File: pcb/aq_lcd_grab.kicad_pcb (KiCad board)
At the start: 4 copper layers, 32 x 50 mm, 29 parts, among them J1 Conn_01x39_Socket, J2 Conn_01x39_Socket, J3 Conn_01x03_Socket, J4 Conn_01x02_Socket, J5 Conn_01x03_Pin, U1 STM32F103C8Tx, U2 Conn_01x14

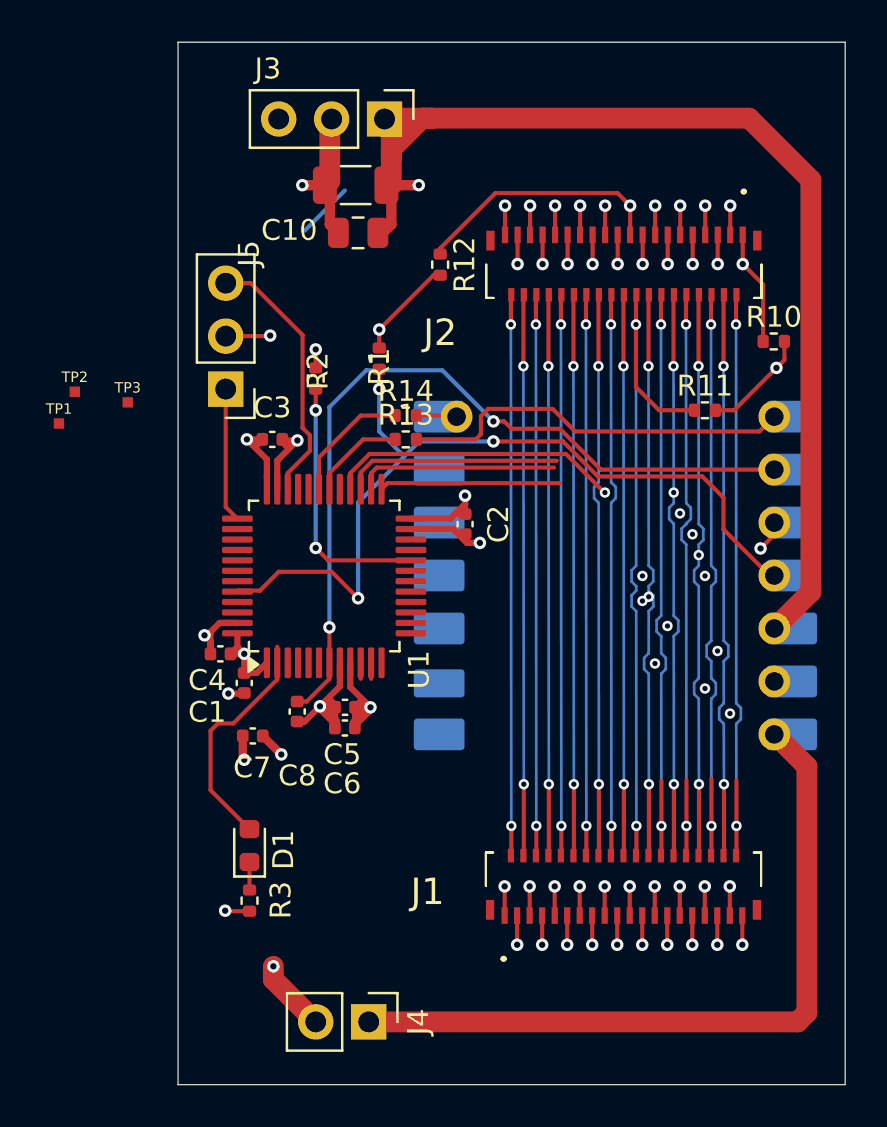
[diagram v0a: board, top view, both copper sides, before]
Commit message: pcb: test points on PA6/7/8; STM32 PA11 as second PIC32 reset driver
- Replace test-point cluster (was PB3/PB4/PA6, required JTAG disable)
  with PA6/PA7/PA8 (pads 16/17/29) — all plain GPIO, no AF conflicts.

- Add STM32 PA11 (pad 32) as a second open-drain driver for PIC32 reset,
  mirroring the existing ESP32 GPIO20 path.  Both drivers wire through
  individual 0 Ω jumpers (R15 = ESP32 side, R16 = STM32 side) onto the
  shared PIC32_RESET net at J3 pin 3; break a jumper to isolate that
  driver without cutting the other.

- Regen netlist and update KiCad PCB with new footprints / net names.

- route_lcd_bus.py: rework escape-via placement (drop odd_db_escape_y
  helper, consolidate into EXTRA_ESCAPE_VIAS with base+step arithmetic).

Co-Authored-By: Claude Sonnet 4.6 <noreply@anthropic.com>
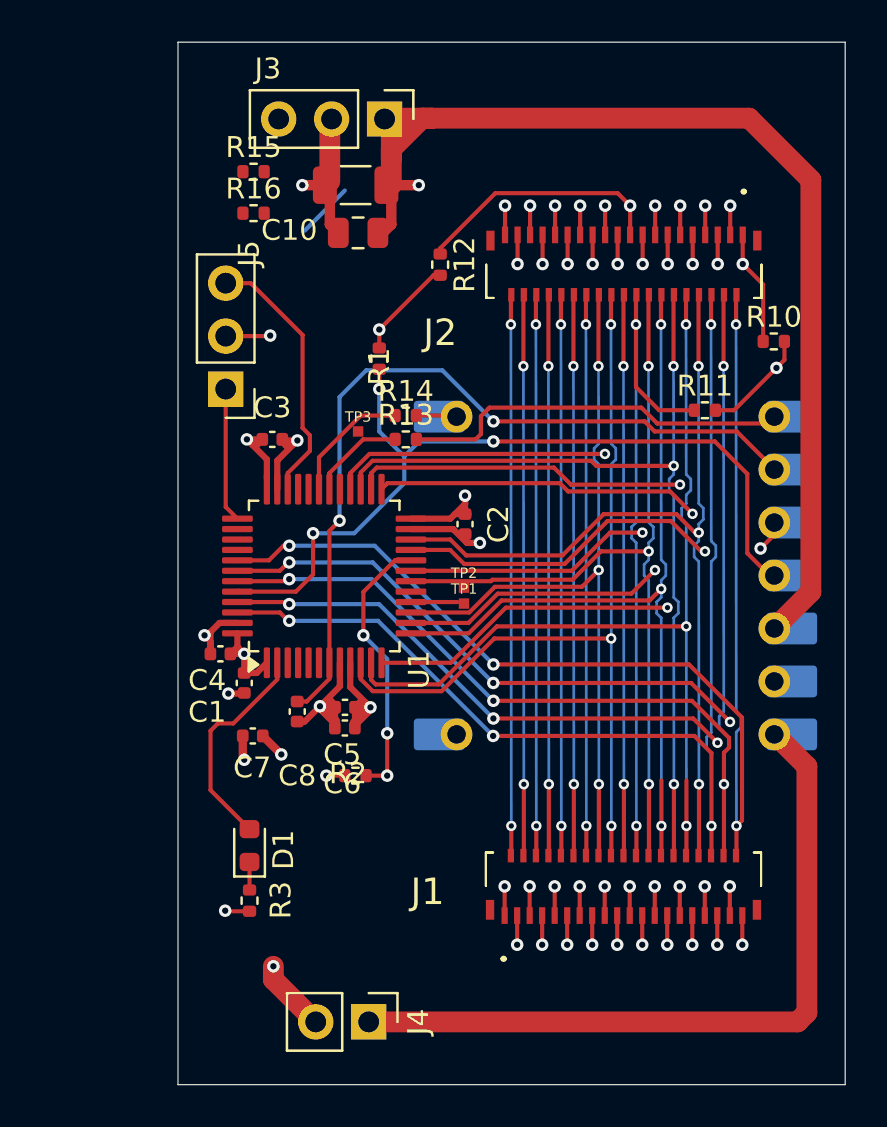
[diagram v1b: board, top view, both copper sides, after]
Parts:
- added R15: 0, Resistor_SMD:R_0402_1005Metric, F.Cu at (54.4, 31.6)
- added R16: 0, Resistor_SMD:R_0402_1005Metric, F.Cu at (54.4, 33.6)
- moved TP1 21.3 mm to (64.5, 52.3)
- moved TP2 20.9 mm to (64.5, 51.6)
- moved R2 19.1 mm to (59.3, 60.6), turned to 180 degrees
- moved TP3 11.1 mm to (59.4, 44.1)
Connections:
- TP1 pad 1: PB3 -> PA6
- TP2 pad 1: PB4 -> PA7
- TP3 pad 1: PA6 -> PA8
- U1 pad 17: (no net) -> PA7
- U1 pad 29: (no net) -> PA8
- U1 pad 32: (no net) -> PIC32_RST_STM
- U1 pad 39: PB3 -> (no net)
- U1 pad 40: PB4 -> (no net)
- U2 pad 10: PIC32_RESET -> PIC32_RST_ESP
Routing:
- net DB0: track 29.3 -> 60.3 mm, vias 2 -> 4
- net DB2: track 27.0 -> 55.9 mm, vias 2 -> 4
- net DB1: track 36.1 -> 63.1 mm, vias 3 -> 5
- net DB4: track 29.7 -> 56.2 mm, vias 2 -> 4
- net DB3: track 36.1 -> 62.0 mm, vias 3 -> 5
- net DB8: track 30.2 -> 46.6 mm, vias 2 -> 3
- net DB5: track 36.3 -> 52.1 mm, vias 4 -> 3
- net DB6: track 27.0 -> 42.2 mm
- net DB11: track 36.3 -> 51.3 mm
- net WR: track 27.8 -> 41.1 mm, vias 2 -> 3
- net DB13: track 36.3 -> 49.2 mm
- net DB12: track 29.4 -> 42.3 mm, vias 2 -> 3
- net DB15: track 36.3 -> 48.2 mm, vias 4 -> 3
- net DB14: track 27.0 -> 38.8 mm
- net CS: track 26.6 -> 36.5 mm, vias 2 -> 3
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
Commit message: pcb: place tooling holes, logo, v1 label; add logo footprint library
- H1–H4 tooling holes placed at board corners (1.152 mm, JLCPCB spec).
- logo:logo-1cm placed on silkscreen.
- v1-<hash> label added to F.SilkS.
- logo.pretty/ added to repo and registered in fp-lib-table.
- kicad_pro: suppress DRC warnings for silk overlap/text height/thickness
  (logo footprint triggers these by design).

Co-Authored-By: Claude Sonnet 4.6 <noreply@anthropic.com>
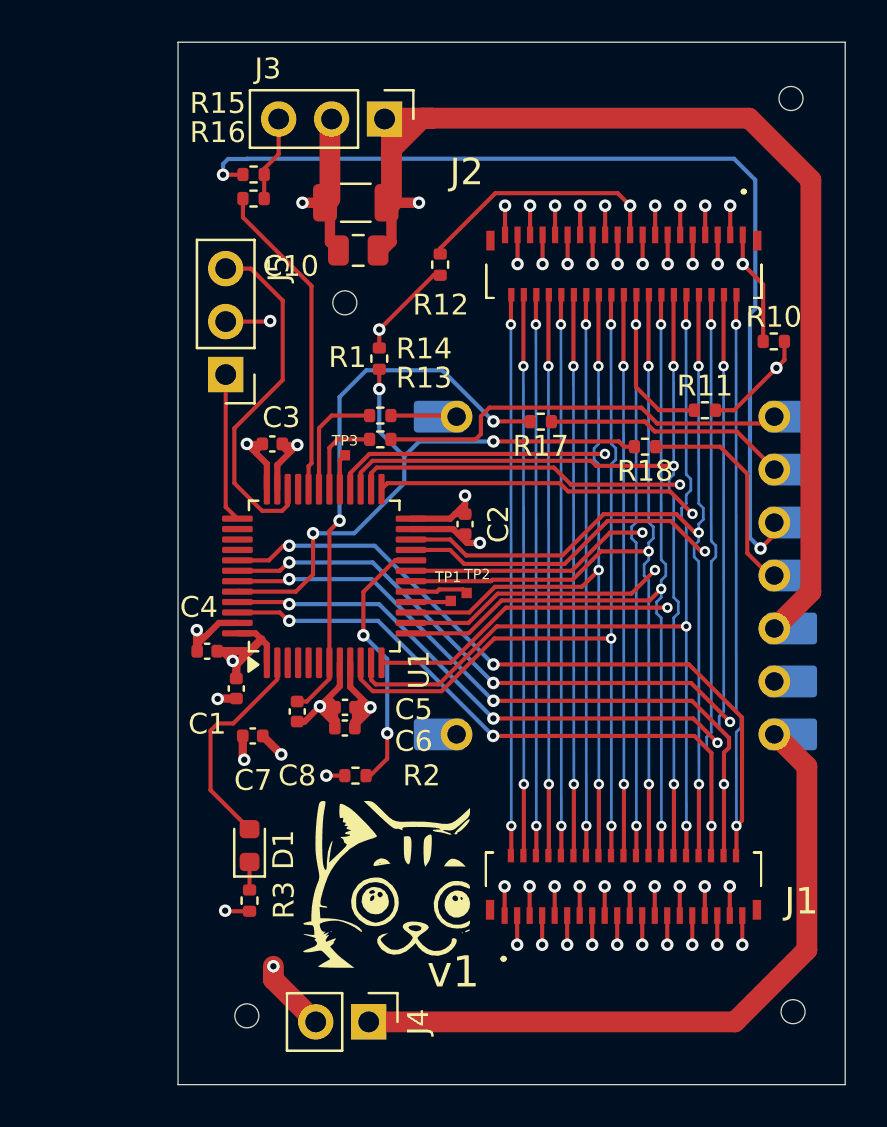
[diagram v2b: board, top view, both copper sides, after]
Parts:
- added H1: ToolingHole, MountingHole:ToolingHole_1.152mm, F.Cu at (58.8, 37.9)
- added H2: ToolingHole, MountingHole:ToolingHole_1.152mm, F.Cu at (54.1, 72.1)
- added H3: ToolingHole, MountingHole:ToolingHole_1.152mm, F.Cu at (80.2, 28.1)
- added H4: ToolingHole, MountingHole:ToolingHole_1.152mm, F.Cu at (80.3, 71.9)
- added R17: 0, Resistor_SMD:R_0402_1005Metric, F.Cu at (68.2, 43.6)
- added R18: 0, Resistor_SMD:R_0402_1005Metric, F.Cu at (73.2, 44.8)
- added v1: LOGO, logo:logo-8mm, F.Cu at (60.8, 65.8)
- added v1: LOGO, logo:logo-2cm, B.Cu at (67.1, 57.5)
- D1: value GREEN -> KT-0603R
- J1, J2: value Conn_01x39_Socket -> FH26W-39S-0.3SHW(60)
- U1: value STM32F103C8Tx -> STM32F103C8T6
- moved TP3 1.31 mm to (58.8, 45.2)
- moved R13 1.22 mm to (60.5, 44.5)
- moved R14 1.22 mm to (60.5, 43.3)
- moved C10 0.84 mm to (59.4, 35.4)
- moved C11 0.84 mm to (59.3, 33.1)
- moved R16 0.70 mm to (54.4, 32.9)
- moved J5 0.70 mm to (53.1, 41.3)
- moved TP1 0.65 mm to (63.9, 52.2)
- moved C4 0.65 mm to (52.2, 54.6)
- moved C1 0.46 mm to (53.6, 56.4)
- moved TP2 0.28 mm to (64.6, 51.8)
- moved C3 0.22 mm to (55.3, 44.7)
- moved R15 0.13 mm to (54.4, 31.7)
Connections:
- U2 pad 11: BOOT0 -> BOOT0_ESP
- U2 pad 9: NRST -> NRST_ESP
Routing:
- net PIC32_RST_ESP: track 1.52 -> 47.0 mm, vias 1 -> 2
- net PIC32_RST_STM: track 0.00 -> 15.4 mm
- net NRST: track 39.1 -> 26.4 mm
- net NRST_ESP: track 0.00 -> 11.7 mm
- net BOOT0: track 40.3 -> 28.8 mm
- net BOOT0_ESP: track 0.00 -> 10.5 mm
- net +3V3: track 76.2 -> 81.7 mm
- net SWDIO: track 12.7 -> 17.1 mm
- net PA7: track 0.00 -> 2.78 mm
- net DB8: track 46.6 -> 44.4 mm
- net DB12: track 42.3 -> 40.1 mm
- net GND: track 43.8 -> 45.7 mm
- net +5V: track 35.2 -> 33.5 mm
- net PA8: track 0.00 -> 1.73 mm
- net PIC32_RESET: track 2.73 -> 4.10 mm
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
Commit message: pcb: update kicad_pcb after LED polarity fix netlist re-import
Co-Authored-By: Claude Sonnet 4.6 <noreply@anthropic.com>
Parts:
- moved R11 1.07 mm to (75.0, 43.1)
- moved R15 0.83 mm to (53.6, 31.7)
- moved R16 0.83 mm to (53.6, 32.9)
- turned D1 to -90 degrees
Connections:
- D1 pad 1: N$1 -> LED_STATUS
- D1 pad 2: LED_STATUS -> N$1
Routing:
- net GND_18: track 33.3 -> 32.2 mm
- net GND: track 45.7 -> 46.8 mm
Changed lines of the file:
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@@
 	(footprint "Resistor_SMD:R_0402_1005Metric"
 		(layer "F.Cu")
-		(at 54.422 32.9)
+		(at 53.59 32.9)
 		(descr "Resistor SMD 0402 (1005 Metric), square (rectangular) end terminal, IPC-7351 nominal, (Body size source: IPC-SM-782 page 72, https://www.pcb-3d.com/wordpress/wp-content/uploads/ipc-sm-782a_amendment_1_and_2.pdf)")
 		(tags "resistor")
 		(property "Reference" "R16"
-			(at -1.717 -3.175 0)
+			(at -0.79 -3.4 0)
 			(layer "F.SilkS")
 			(effects
@@
 	(footprint "Resistor_SMD:R_0402_1005Metric"
 		(layer "F.Cu")
-		(at 54.422 31.744)
+		(at 53.59 31.744)
 		(descr "Resistor SMD 0402 (1005 Metric), square (rectangular) end terminal, IPC-7351 nominal, (Body size source: IPC-SM-782 page 72, https://www.pcb-3d.com/wordpress/wp-content/uploads/ipc-sm-782a_amendment_1_and_2.pdf)")
 		(tags "resistor")
 		(property "Reference" "R15"
-			(at -1.717 -3.416 0)
+			(at -0.79 -3.544 0)
 			(layer "F.SilkS")
 			(effects
@@
 		(tags "Through hole pin header THT 1x03 2.54mm single row")
 		(property "Reference" "J5"
-			(at -2.54 5.08 90)
+			(at -2.314 0.34 90)
 			(layer "F.SilkS")
 			(effects
@@
 		(tags "capacitor")
 		(property "Reference" "C10"
-			(at 3.236 -0.756 0)
+			(at 3.243 0.388 0)
 			(layer "F.SilkS")
 			(effects
@@
 	(footprint "LED_SMD:LED_0603_1608Metric"
 		(layer "F.Cu")
-		(at 54.229 63.932 90)
+		(at 54.229 63.932 -90)
 		(descr "LED SMD 0603 (1608 Metric), square (rectangular) end terminal, IPC-7351 nominal, (Body size source: http://www.tortai-tech.com/upload/download/2011102023233369053.pdf)")
 		(tags "LED")
@@
 		)
 		(property "SKiDL Tag" "D1_LED_STATUS"
-			(at 0 0 90)
+			(at 0 0 270)
 			(unlocked yes)
 			(layer "F.Fab")
@@
 		)
 		(property "SKiDL Line" "aq_lcd_grab.py:399"
-			(at 0 0 90)
+			(at 0 0 270)
 			(unlocked yes)
 			(layer "F.Fab")
@@
 		(duplicate_pad_numbers_are_jumpers no)
 		(fp_line
-			(start 0.8 -0.735)
-			(end -1.485 -0.735)
+			(start -1.485 0.735)
+			(end 0.8 0.735)
 			(stroke
 				(width 0.12)
@@
 		)
 		(fp_line
-			(start -1.485 0.735)
-			(end 0.8 0.735)
+			(start 0.8 -0.735)
+			(end -1.485 -0.735)
 			(stroke
 				(width 0.12)
@@
 		)
 		(fp_line
-			(start 0.8 -0.4)
-			(end -0.5 -0.4)
+			(start -0.8 0.4)
+			(end 0.8 0.4)
 			(stroke
 				(width 0.1)
@@
 		)
 		(fp_line
-			(start -0.5 -0.4)
-			(end -0.8 -0.1)
+			(start 0.8 0.4)
+			(end 0.8 -0.4)
 			(stroke
 				(width 0.1)
@@
 		)
 		(fp_line
-			(start 0.8 0.4)
-			(end 0.8 -0.4)
+			(start -0.5 -0.4)
+			(end -0.8 -0.1)
 			(stroke
 				(width 0.1)
@@
 		)
 		(fp_line
-			(start -0.8 0.4)
-			(end 0.8 0.4)
+			(start 0.8 -0.4)
+			(end -0.5 -0.4)
 			(stroke
 				(width 0.1)
@@
 		)
 		(pad "1" smd roundrect
-			(at -0.7875 0 90)
+			(at -0.7875 0 270)
 			(size 0.875 0.95)
 			(layers "F.Cu" "F.Mask" "F.Paste")
 			(roundrect_rratio 0.25)
-			(net "N$1")
+			(net "LED_STATUS")
 			(pintype "PASSIVE")
 		)
 		(pad "2" smd roundrect
-			(at 0.7875 0 90)
+			(at 0.7875 0 270)
 			(size 0.875 0.95)
 			(layers "F.Cu" "F.Mask" "F.Paste")
 			(roundrect_rratio 0.25)
-			(net "LED_STATUS")
+			(net "N$1")
 			(pintype "PASSIVE")
 		)
@@
 	(footprint "Resistor_SMD:R_0402_1005Metric"
 		(layer "F.Cu")
-		(at 76.071 43.053)
+		(at 75 43.053)
 		(descr "Resistor SMD 0402 (1005 Metric), square (rectangular) end terminal, IPC-7351 nominal, (Body size source: IPC-SM-782 page 72, https://www.pcb-3d.com/wordpress/wp-content/uploads/ipc-sm-782a_amendment_1_and_2.pdf)")
 		(tags "resistor")
@@
 	)
 	(segment
-		(start 79.502 41.021)
-		(end 77.47 43.053)
-		(width 0.2)
-		(layer "F.Cu")
-		(net "GND")
-	)
-	(segment
 		(start 52.208501 53.808501)
 		(end 51.717 54.300001)
@@
 	)
 	(segment
-		(start 77.47 43.053)
-		(end 76.581 43.053)
-		(width 0.2)
-		(layer "F.Cu")
-		(net "GND")
-	)
-	(segment
 		(start 55.56 45.68195)
 		(end 56.5239 44.71805)
@@
 	)
 	(segment
+		(start 75.51 43.053)
+		(end 77.47 43.053)
+		(width 0.2)
+		(layer "F.Cu")
+		(net "GND")
+	)
+	(segment
 		(start 63.9925 48.7525)
 		(end 64.6558 49.4158)
@@
 	)
 	(segment
+		(start 77.47 43.053)
+		(end 79.502 41.021)
+		(width 0.2)
+		(layer "F.Cu")
+		(net "GND")
+	)
+	(segment
 		(start 58.086 34.988)
 		(end 58.611 35.513)
@@
 	)
 	(segment
-		(start 57.2 37.088)
-		(end 53.912 33.8)
+		(start 53.08 32.968)
+		(end 57.2 37.088)
 		(width 0.2)
 		(layer "F.Cu")
@@
 	)
 	(segment
-		(start 57.2 45.6)
-		(end 57.2 37.088)
+		(start 53.08 32.9)
+		(end 53.08 32.968)
 		(width 0.2)
 		(layer "F.Cu")
@@
 	)
 	(segment
-		(start 53.912 33.8)
-		(end 53.912 32.9)
+		(start 57.2 45.6)
+		(end 57.2 37.088)
 		(width 0.2)
 		(layer "F.Cu")
@@
 	)
 	(segment
-		(start 55.626 30.774)
-		(end 55.626 29.083)
+		(start 54.1 32.9)
+		(end 54.1 31.744)
 		(width 0.2)
 		(layer "F.Cu")
@@
 	)
 	(segment
-		(start 54.932 32.9)
-		(end 54.932 31.744)
+		(start 55.626 29.083)
+		(end 54.1 30.609)
 		(width 0.2)
 		(layer "F.Cu")
@@
 	)
 	(segment
-		(start 54.932 31.468)
-		(end 55.626 30.774)
-		(width 0.2)
-		(layer "F.Cu")
-		(net "PIC32_RESET")
-	)
-	(segment
-		(start 54.932 31.744)
-		(end 54.932 31.468)
+		(start 54.1 30.609)
+		(end 54.1 31.744)
 		(width 0.2)
 		(layer "F.Cu")
@@
 	)
 	(segment
-		(start 75.561 43.053)
-		(end 73.877572 43.053)
+		(start 72.765032 37.54)
+		(end 72.765032 38.94)
 		(width 0.2)
 		(layer "F.Cu")
@@
 	)
 	(segment
-		(start 72.765032 37.54)
-		(end 72.765032 38.94)
+		(start 73.877572 43.053)
+		(end 74.49 43.053)
 		(width 0.2)
 		(layer "F.Cu")
@@
 	)
 	(segment
-		(start 53.899 31.757)
-		(end 53.912 31.744)
+		(start 79.4 48.44)
+		(end 79.4 49.0224)
 		(width 0.2)
 		(layer "F.Cu")
@@
 	)
 	(segment
-		(start 79.4 48.44)
-		(end 79.4 49.0224)
+		(start 79.4 49.0224)
+		(end 78.74 49.6824)
 		(width 0.2)
 		(layer "F.Cu")
@@
 	)
 	(segment
-		(start 79.4 49.0224)
-		(end 78.74 49.6824)
+		(start 53.08 30.58)
+		(end 52.9 30.4)
 		(width 0.2)
 		(layer "F.Cu")
@@
 	)
 	(segment
-		(start 52.959 31.757)
-		(end 53.899 31.757)
+		(start 53.08 31.744)
+		(end 53.08 30.58)
 		(width 0.2)
 		(layer "F.Cu")
@@
 	)
 	(via
-		(at 52.959 31.757)
+		(at 52.9 30.4)
 		(size 0.6)
 		(drill 0.3)
@@
 	)
 	(segment
-		(start 77.47 30.988)
-		(end 78.485032 32.003032)
-		(width 0.2)
-		(layer "B.Cu")
-		(net "PIC32_RST_ESP")
-	)
-	(segment
-		(start 54.112 30.988)
-		(end 54.1 31)
+		(start 78.232 38.435497)
+		(end 78.232 49.1744)
 		(width 0.2)
 		(layer "B.Cu")
@@
 	)
 	(segment
-		(start 54.112 30.988)
-		(end 77.47 30.988)
+		(start 52.9 30.4)
+		(end 53.488 30.988)
 		(width 0.2)
 		(layer "B.Cu")
@@
 	)
 	(segment
-		(start 78.232 49.1744)
-		(end 78.74 49.6824)
-		(width 0.2)
-		(layer "B.Cu")
-		(net "PIC32_RST_ESP")
-	)
-	(segment
-		(start 78.232 38.435497)
-		(end 78.232 49.1744)
-		(width 0.2)
-		(layer "B.Cu")
-		(net "PIC32_RST_ESP")
-	)
-	(segment
-		(start 54.1 31)
-		(end 53.2 31)
+		(start 77.47 30.988)
+		(end 78.485032 32.003032)
 		(width 0.2)
 		(layer "B.Cu")
@@
 	)
 	(segment
-		(start 53.2 31)
-		(end 52.959 31.241)
+		(start 53.488 30.988)
+		(end 77.47 30.988)
 		(width 0.2)
 		(layer "B.Cu")
@@
 	)
 	(segment
-		(start 52.959 31.757)
-		(end 52.959 31.241)
+		(start 78.232 49.1744)
+		(end 78.74 49.6824)
 		(width 0.2)
 		(layer "B.Cu")
